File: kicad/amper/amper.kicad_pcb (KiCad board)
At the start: 2 copper layers, 80 x 99 mm, 59 parts, among them J1 Conn_02x05_Odd_Even, J2 Conn_02x05_Odd_Even, J3 Conn_02x05_Odd_Even, J4 USB_C_Receptacle_USB2.0, J5 Conn_01x03, J6 Conn_01x04, J7 Conn_01x05, J8 Conn_01x09, J9 Conn_01x09, Q1 FDS9435A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

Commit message: Rev C appears finished, going to sleep on it
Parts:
- added R17: 500, Resistor_SMD:R_0603_1608Metric_Pad1.05x0.95mm_HandSolder, F.Cu at (-14.0, 23.2)
- added R18: 500, Resistor_SMD:R_0603_1608Metric_Pad1.05x0.95mm_HandSolder, F.Cu at (32.0, 23.2)
- added R19: 10K, Resistor_SMD:R_0603_1608Metric_Pad1.05x0.95mm_HandSolder, F.Cu at (18.0, -24.0)
- added R20: 10K, Resistor_SMD:R_0603_1608Metric_Pad1.05x0.95mm_HandSolder, F.Cu at (20.0, -24.0)
- R13, R14: value 100K -> 500
- R7, R8: value 30k -> 15k
- U5: value 114-87-308-41-134161 -> 114-87-308-41-134161 (MCP602-E/P)
- moved J1 2.00 mm to (0.00, 35.0)
- moved J3 2.00 mm to (0.00, 11.0)
- moved U5 2.00 mm to (0.00, -3.24)
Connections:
- J1 pad 9: /ResultAdc -> /ResultOut
- J7 pad 5: /ResultAdc -> /ResultOut
- J9 pad 7: /SourceAOut -> /SourceAAdc
- J9 pad 8: /SourceBOut -> /SourceBAdc
- R13 pad 2: GND -> /SourceAAdc
- R14 pad 2: GND -> /SourceBAdc
- U5 pad 1: Net-(U5-Pad1) -> /ResultOut
- U5 pad 5: Net-(U5-Pad5) -> GND
- U5 pad 6: /ResultAdc -> +5V
- U5 pad 7: +5V -> Net-(U5-Pad7)
- U5 pad 8: Net-(U5-Pad8) -> +5V
- U7 pad 17: /SourceAOut -> /SourceAAdc
- U7 pad 18: /SourceBOut -> /SourceBAdc
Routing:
- net /SourceAAdc: track 0.00 -> 96.2 mm, vias 0 -> 3
- net /ResultOut: track 0.00 -> 94.2 mm, vias 0 -> 2
- net /SourceAOut: track 139.5 -> 47.8 mm, vias 4 -> 2
- net /ResultAdc: track 108.9 -> 20.1 mm, vias 2 -> 0
- net /SourceBAdc: track 0.00 -> 74.5 mm, vias 0 -> 2
- net /SourceBOut: track 130.0 -> 58.8 mm, vias 3 -> 2
- net GND: track 109.4 -> 103.2 mm, vias 17 -> 19
- net /R5: track 17.6 -> 21.6 mm
- net /R3: track 17.6 -> 21.6 mm
- net /R1: track 17.6 -> 21.6 mm
- net /R4: track 11.6 -> 15.6 mm
- net /R2: track 11.6 -> 15.6 mm
- net /V+: track 12.1 -> 11.5 mm
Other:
- board text added: "Amper Rev C"
- board text removed: "Amper Rev B"

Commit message: cleanup
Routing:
- net /SourceBAdc: vias 2 -> 1
- net /SourceAAdc: vias 3 -> 2

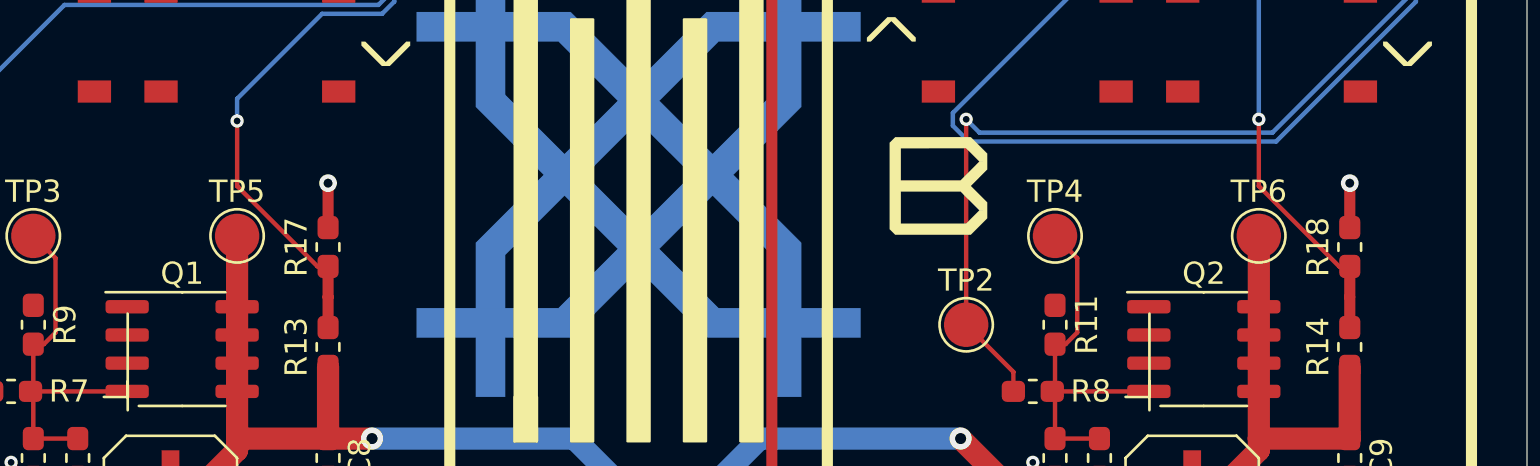
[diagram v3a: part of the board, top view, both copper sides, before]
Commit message: Added an extra button to the pcb
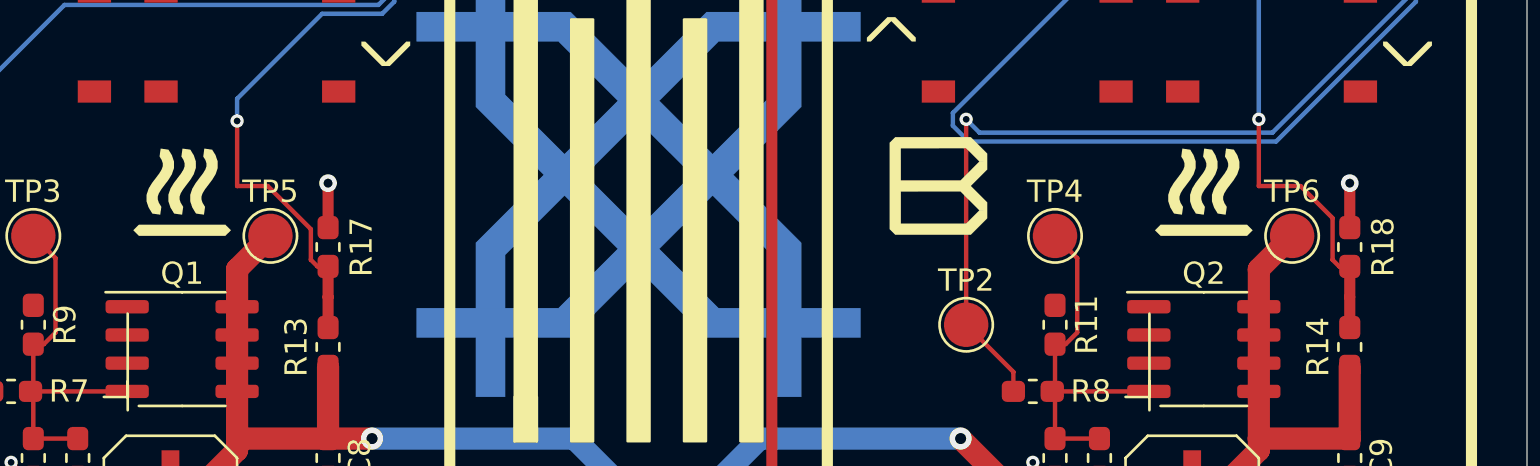
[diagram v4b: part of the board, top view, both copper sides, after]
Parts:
- added svg2mod: G***, amper:LargeHeatWarning, F.Cu at (25.4, 20.5)
- added svg2mod: G***, amper:LargeHeatWarning, F.Cu at (-20.6, 20.5)
- moved TP5 1.50 mm to (-16.6, 22.8)
- moved TP6 1.50 mm to (29.4, 22.8)
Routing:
- net /SourceBAdc: track 74.5 -> 75.6 mm
- net /SourceBOut: track 58.8 -> 59.7 mm
- net /SourceAOut: track 47.8 -> 48.7 mm
- net /SourceAAdc: track 96.2 -> 97.0 mm

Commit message: PCB tidy pass
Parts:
- added R21: 10K, Resistor_SMD:R_0603_1608Metric_Pad1.05x0.95mm_HandSolder, F.Cu at (21.5, -17.4)
- added SW5: SW_Push, amper:K2-1157SP-I4SW-01, F.Cu at (27.5, -16.0)
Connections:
- net Net-(J8-Pad1) renamed /AuxButton
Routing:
- net /AuxButton: track 9.56 -> 29.4 mm
- net /SEG5: track 110.5 -> 107.6 mm
- net /SourceBDigit2: track 89.0 -> 86.5 mm
- net /SEG6: track 104.7 -> 102.6 mm
- net GND: track 103.2 -> 104.9 mm, vias 19 -> 20

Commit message: Replotted rev C
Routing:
- net GND: track 104.9 -> 104.3 mm
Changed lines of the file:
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@@
     (thickness 1.6)
     (drawings 33)
-    (tracks 735)
+    (tracks 733)
     (zones 0)
     (modules 67)
@@
   )
   (setup
-    (last_trace_width 0.2)
+    (last_trace_width 0.5)
     (user_trace_width 0.2)
     (user_trace_width 0.5)
@@
   (segment (start -30 -37.375) (end -29.375 -38) (width 0.5) (layer F.Cu) (net 1) (status 20))
   (segment (start -30 -35.715) (end -30 -37.375) (width 0.5) (layer F.Cu) (net 1) (status 10))
-  (via (at -13.5 -30.5) (size 0.6) (drill 0.3) (layers F.Cu B.Cu) (net 1))
-  (segment (start -16.91 -30.5) (end -13.5 -30.5) (width 0.2) (layer F.Cu) (net 1))
   (segment (start -17.23 -30.18) (end -16.91 -30.5) (width 0.2) (layer F.Cu) (net 1) (status 10))
   (segment (start -17.23 -29.655) (end -17.23 -30.18) (width 0.2) (layer F.Cu) (net 1) (status 30))
@@
   (segment (start -2.54 36.774) (end -2.54 34.6) (width 0.5) (layer F.Cu) (net 1) (status 10))
   (via (at -2.54 34.6) (size 0.8) (drill 0.4) (layers F.Cu B.Cu) (net 1))
-  (segment (start 21.5 -15.975) (end 21.5 -14.8) (width 0.2) (layer F.Cu) (net 1))
-  (segment (start 21.5 -16.5) (end 21.5 -15.975) (width 0.2) (layer F.Cu) (net 1))
-  (segment (start 21.5 -14.8) (end 21.5 -14.8) (width 0.2) (layer F.Cu) (net 1))
-  (via (at 21.5 -14.8) (size 0.6) (drill 0.3) (layers F.Cu B.Cu) (net 1))
+  (segment (start 21.5 -16.5) (end 23.5 -16.5) (width 0.2) (layer F.Cu) (net 1))
+  (via (at 23.5 -16.5) (size 0.6) (drill 0.3) (layers F.Cu B.Cu) (net 1))
+  (via (at -14.551417 -30.80315) (size 0.6) (drill 0.3) (layers F.Cu B.Cu) (net 1))
+  (segment (start -14.854567 -30.5) (end -14.551417 -30.80315) (width 0.2) (layer F.Cu) (net 1))
+  (segment (start -16.91 -30.5) (end -14.854567 -30.5) (width 0.2) (layer F.Cu) (net 1))
   (segment (start -26.52 45) (end -26.52 44) (width 0.8) (layer F.Cu) (net 2) (status 10))
   (segment (start -23.48 45) (end -23.48 43.9) (width 0.8) (layer F.Cu) (net 2) (status 10))
@@
   (segment (start -30 -15) (end -30 -24.285) (width 0.5) (layer F.Cu) (net 12) (status 20))
   (segment (start -28.08 -13.08) (end -30 -15) (width 0.5) (layer F.Cu) (net 12))
-  (segment (start 25.54 7.4) (end 25.54 3.5) (width 0.5) (layer F.Cu) (net 13) (status 10))
   (segment (start 2.54 -16.6) (end 2.54 -12) (width 0.5) (layer F.Cu) (net 13) (status 10))
-  (segment (start 17.090001 -4.949999) (end 25.54 3.5) (width 0.5) (layer F.Cu) (net 13))
-  (segment (start 9.590001 -4.949999) (end 17.090001 -4.949999) (width 0.5) (layer F.Cu) (net 13))
-  (segment (start 2.54 -12) (end 9.590001 -4.949999) (width 0.5) (layer F.Cu) (net 13))
   (via (at 2.54 -12) (size 0.8) (drill 0.4) (layers F.Cu B.Cu) (net 13))
   (segment (start -20.46 7.4) (end -20.46 4) (width 0.5) (layer F.Cu) (net 13) (status 10))
@@
   (segment (start -5.659982 -28.607909) (end -3.81786 -30.450031) (width 0.5) (layer B.Cu) (net 13))
   (segment (start -5.659982 -28.339866) (end -5.659982 -28.607909) (width 0.5) (layer B.Cu) (net 13))
+  (segment (start 25.54 3.780002) (end 25.54 7.4) (width 0.5) (layer F.Cu) (net 13))
+  (segment (start 9.759998 -12) (end 25.54 3.780002) (width 0.5) (layer F.Cu) (net 13))
+  (segment (start 2.54 -12) (end 9.759998 -12) (width 0.5) (layer F.Cu) (net 13))
   (segment (start 0 -12) (end 0 -16.6) (width 0.5) (layer F.Cu) (net 14) (status 20))
   (via (at 0 -12) (size 0.8) (drill 0.4) (layers F.Cu B.Cu) (net 14))
@@
   (segment (start -15.209896 -17.79999) (end -4.959972 -28.049914) (width 0.5) (layer B.Cu) (net 14))
   (segment (start -4.959972 -28.317956) (end -3.527907 -29.750021) (width 0.5) (layer B.Cu) (net 14))
-  (segment (start 3.299978 -8.700022) (end 4.850022 -8.700022) (width 0.5) (layer F.Cu) (net 14))
-  (segment (start 23 1.949962) (end 23 7.4) (width 0.5) (layer F.Cu) (net 14) (status 20))
-  (segment (start 16.800048 -4.24999) (end 23 1.949962) (width 0.5) (layer F.Cu) (net 14))
-  (segment (start 9.300052 -4.249991) (end 16.800048 -4.24999) (width 0.5) (layer F.Cu) (net 14))
-  (segment (start 4.850022 -8.700022) (end 9.300052 -4.249991) (width 0.5) (layer F.Cu) (net 14))
-  (segment (start 0 -12) (end 3.299978 -8.700022) (width 0.5) (layer F.Cu) (net 14))
+  (segment (start 23 2.229964) (end 23 7.4) (width 0.5) (layer F.Cu) (net 14))
+  (segment (start 0.850001 -11.149999) (end 9.620037 -11.149999) (width 0.5) (layer F.Cu) (net 14))
+  (segment (start 9.620037 -11.149999) (end 23 2.229964) (width 0.5) (layer F.Cu) (net 14))
+  (segment (start 0 -12) (end 0.850001 -11.149999) (width 0.5) (layer F.Cu) (net 14))
   (segment (start -2.54 -12) (end -2.54 -16.6) (width 0.5) (layer F.Cu) (net 15) (status 20))
   (segment (start -2.52 -11.98) (end -2.54 -12) (width 0.5) (layer F.Cu) (net 15))
@@
   (segment (start -4.259962 -28.028003) (end -3.237954 -29.050011) (width 0.5) (layer B.Cu) (net 15))
   (segment (start -4.259962 -27.759962) (end -4.259962 -28.028003) (width 0.5) (layer B.Cu) (net 15))
-  (segment (start 1.459989 -8.000011) (end -2.52 -11.98) (width 0.5) (layer F.Cu) (net 15))
-  (segment (start 20.46 7.4) (end 20.46 0.470035) (width 0.5) (layer F.Cu) (net 15) (status 10))
-  (segment (start 16.439985 -3.54998) (end 9.010099 -3.54998) (width 0.5) (layer F.Cu) (net 15))
-  (segment (start 4.560068 -8.000011) (end 1.459989 -8.000011) (width 0.5) (layer F.Cu) (net 15))
-  (segment (start 9.010099 -3.54998) (end 4.560068 -8.000011) (width 0.5) (layer F.Cu) (net 15))
-  (segment (start 20.46 0.470035) (end 16.439985 -3.54998) (width 0.5) (layer F.Cu) (net 15))
+  (segment (start -2.120001 -11.580001) (end -2.52 -11.98) (width 0.5) (layer F.Cu) (net 15))
+  (segment (start -1.689999 -11.149999) (end -2.120001 -11.580001) (width 0.5) (layer F.Cu) (net 15))
+  (segment (start 0.560048 -10.449989) (end -0.139961 -11.149999) (width 0.5) (layer F.Cu) (net 15))
+  (segment (start 9.330085 -10.449989) (end 0.560048 -10.449989) (width 0.5) (layer F.Cu) (net 15))
+  (segment (start 20.46 0.679926) (end 9.330085 -10.449989) (width 0.5) (layer F.Cu) (net 15))
+  (segment (start -0.139961 -11.149999) (end -1.689999 -11.149999) (width 0.5) (layer F.Cu) (net 15))
+  (segment (start 20.46 7.4) (end 20.46 0.679926) (width 0.5) (layer F.Cu) (net 15))
   (segment (start -5.08 -12) (end -5.08 -16.6) (width 0.5) (layer F.Cu) (net 16) (status 20))
   (segment (start -5 -12) (end -5.08 -12) (width 0.5) (layer F.Cu) (net 16))
@@
   (segment (start 5.930001 -27.091999) (end 2.237972 -23.39997) (width 0.5) (layer B.Cu) (net 16))
   (segment (start 2.237972 -23.39997) (end -2.680182 -23.39997) (width 0.5) (layer B.Cu) (net 16))
-  (segment (start 7.489973 -4.080141) (end 4.270114 -7.3) (width 0.5) (layer F.Cu) (net 16))
-  (segment (start 16.150031 -2.849969) (end 8.720142 -2.849969) (width 0.5) (layer F.Cu) (net 16))
-  (segment (start 4.270114 -7.3) (end -0.3 -7.3) (width 0.5) (layer F.Cu) (net 16))
-  (segment (start 17.92 7.4) (end 17.92 -1.08) (width 0.5) (layer F.Cu) (net 16) (status 10))
-  (segment (start 8.720142 -2.849969) (end 7.489973 -4.080141) (width 0.5) (layer F.Cu) (net 16))
-  (segment (start 17.92 -1.08) (end 16.150031 -2.849969) (width 0.5) (layer F.Cu) (net 16))
-  (segment (start -0.3 -7.3) (end -5 -12) (width 0.5) (layer F.Cu) (net 16))
+  (segment (start 17.92 -0.78) (end 17.92 7.4) (width 0.5) (layer F.Cu) (net 16))
+  (segment (start 8.950021 -9.749979) (end 17.92 -0.78) (width 0.5) (layer F.Cu) (net 16))
+  (segment (start 0.270095 -9.749979) (end 8.950021 -9.749979) (width 0.5) (layer F.Cu) (net 16))
+  (segment (start -0.429914 -10.449989) (end 0.270095 -9.749979) (width 0.5) (layer F.Cu) (net 16))
+  (segment (start -1.979952 -10.449989) (end -0.429914 -10.449989) (width 0.5) (layer F.Cu) (net 16))
+  (segment (start -4.129999 -11.129999) (end -2.659961 -11.129999) (width 0.5) (layer F.Cu) (net 16))
+  (segment (start -2.659961 -11.129999) (end -1.979952 -10.449989) (width 0.5) (layer F.Cu) (net 16))
+  (segment (start -5 -12) (end -4.129999 -11.129999) (width 0.5) (layer F.Cu) (net 16))
   (segment (start -27.25 27.625) (end -27.25 29.625) (width 0.2) (layer F.Cu) (net 17) (status 30))
   (segment (start -27.25 29.875) (end -27.375 29.75) (width 0.2) (layer F.Cu) (net 17) (status 30))
@@
   (segment (start 28.32501 10.82501) (end 28.32501 -27.98501) (width 0.2) (layer B.Cu) (net 44))
   (segment (start 34 11.75) (end 29.25 11.75) (width 0.2) (layer B.Cu) (net 44))
-  (segment (start 14.55 -21) (end 15.450021 -21.900021) (width 0.2) (layer F.Cu) (net 55))
-  (segment (start 13.5 -21) (end 14.55 -21) (width 0.2) (layer F.Cu) (net 55) (status 10))
-  (segment (start 15.450021 -21.900021) (end 15.450021 -26.350021) (width 0.2) (layer F.Cu) (net 55))
-  (segment (start 16.385 -27.285) (end 17.85 -27.285) (width 0.2) (layer F.Cu) (net 55) (status 20))
-  (segment (start 15.450021 -26.350021) (end 16.385 -27.285) (width 0.2) (layer F.Cu) (net 55))
   (segment (start 15.975 -31.095) (end 13.5 -28.62) (width 0.2) (layer F.Cu) (net 48) (status 20))
   (segment (start 17.85 -31.095) (end 15.975 -31.095) (width 0.2) (layer F.Cu) (net 48) (status 10))
@@
   (segment (start 0.40002 2.254018) (end 0.40002 -1.67998) (width 0.5) (layer F.Cu) (net 54))
   (segment (start 0.40002 -1.67998) (end -1.7 -3.78) (width 0.5) (layer F.Cu) (net 54))
+  (segment (start 14.55 -21) (end 15.450021 -21.900021) (width 0.2) (layer F.Cu) (net 55))
+  (segment (start 13.5 -21) (end 14.55 -21) (width 0.2) (layer F.Cu) (net 55) (status 10))
+  (segment (start 15.450021 -21.900021) (end 15.450021 -26.350021) (width 0.2) (layer F.Cu) (net 55))
+  (segment (start 16.385 -27.285) (end 17.85 -27.285) (width 0.2) (layer F.Cu) (net 55) (status 20))
+  (segment (start 15.450021 -26.350021) (end 16.385 -27.285) (width 0.2) (layer F.Cu) (net 55))
   (segment (start 23.5 -18.25) (end 21.5 -18.25) (width 0.2) (layer F.Cu) (net 55))
   (segment (start 21.5 -18.25) (end 21.025 -18.25) (width 0.2) (layer F.Cu) (net 55))
